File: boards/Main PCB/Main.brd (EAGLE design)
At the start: 101.6 x 76.2 mm, 120 parts, among them CN1 MINIB, CN2 MINIB, IC1 FT232RL, IC2 FT232RL, IC4 OKR-T_3-W12-C, J1 3_PIN_JST-XH, J2 2_PIN_JST-XH, J3 5_PIN_JST-XH, Q4 BSS138, Q5 BSS138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

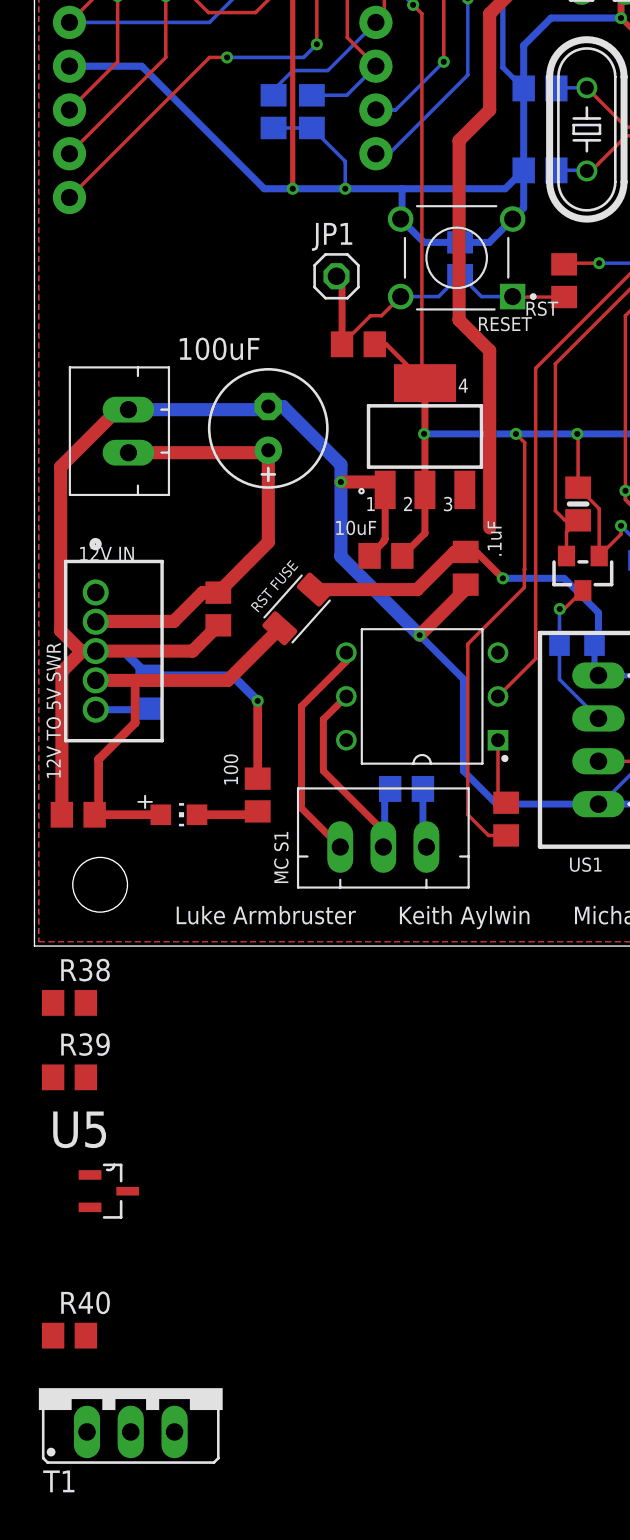
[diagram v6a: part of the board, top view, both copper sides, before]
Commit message: Routed crowbar circuit
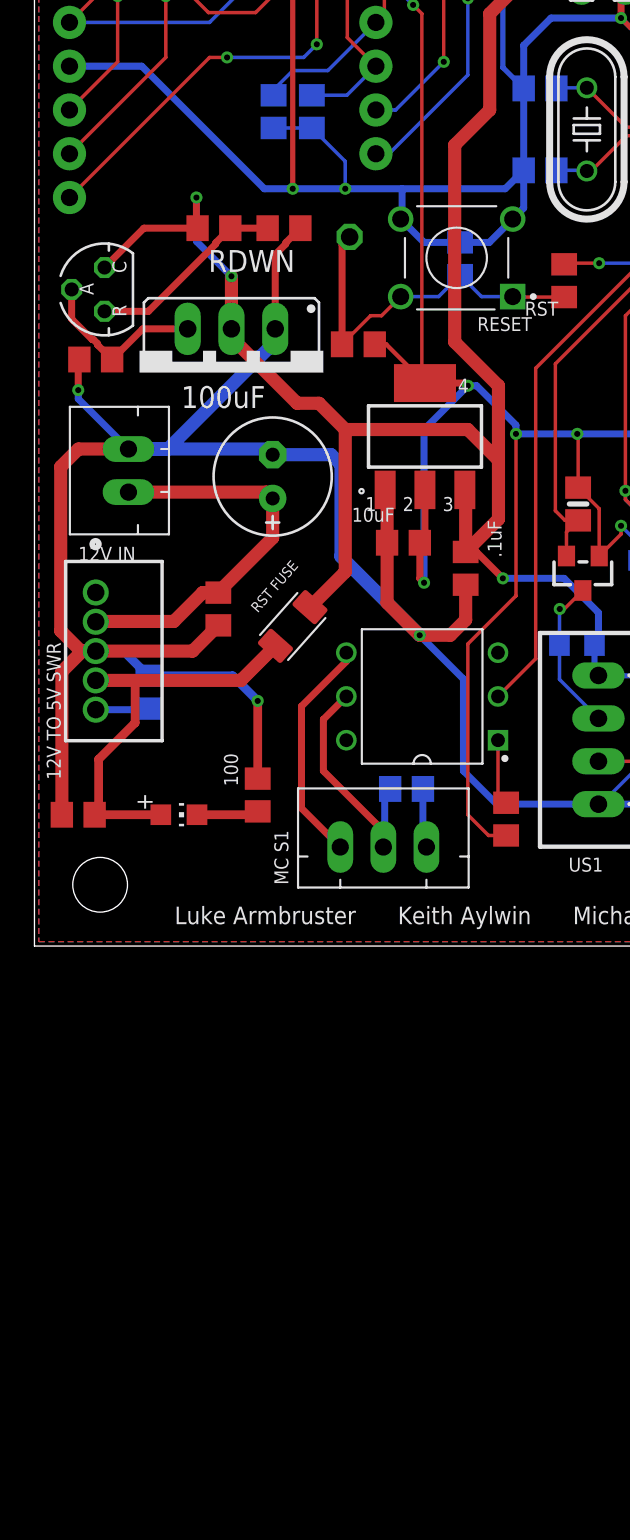
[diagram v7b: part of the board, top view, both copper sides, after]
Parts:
- removed R38, R39: (no value), resistor:R0805
- removed U5: TL431AIDBZTG4, main_library:SOT95P237X112-3N
- added RDWN, RUP: (no value), resistor:R0805
- added VR1: (no value), v-reg:TO92-CLP
- moved T1 59.2 mm to (11.4, 33.3), turned to 180 degrees
- moved R40 56.7 mm to (3.56, 34.0)
- moved C17 2.81 mm to (13.8, 27.2)
- moved JP1 2.41 mm to (18.3, 41.1), flipped to the bottom
- moved J2 2.29 mm to (2.05, 31.3)
- moved C9 1.27 mm to (21.4, 23.4)
- moved R33 1.05 mm to (15.0, 18.5)
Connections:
- removed net N$30: R40.2, T1.G, U5.3
- new net N$24: R40.2, T1.G, VR1.A
- net +5V: now also RUP.2, VR1.C; no longer R38.2, U5.1
- net GND: now also RDWN.1; no longer R39.1
- net N$25: now also RDWN.2, RUP.1, VR1.R; no longer R38.1, R39.2, U5.2
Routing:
- net +5V: track 167.0 -> 210.8 mm, vias 3 -> 5
- net GND: track 764.5 -> 790.5 mm
- net N$25: track 0.00 -> 11.5 mm
- net N$24: track 0.00 -> 10.2 mm
- net +3V3: track 326.9 -> 335.5 mm, vias 21 -> 22
- net RESET: track 19.2 -> 21.5 mm
- net 12V_IN: track 25.4 -> 23.1 mm
- net N$21: track 26.7 -> 26.1 mm

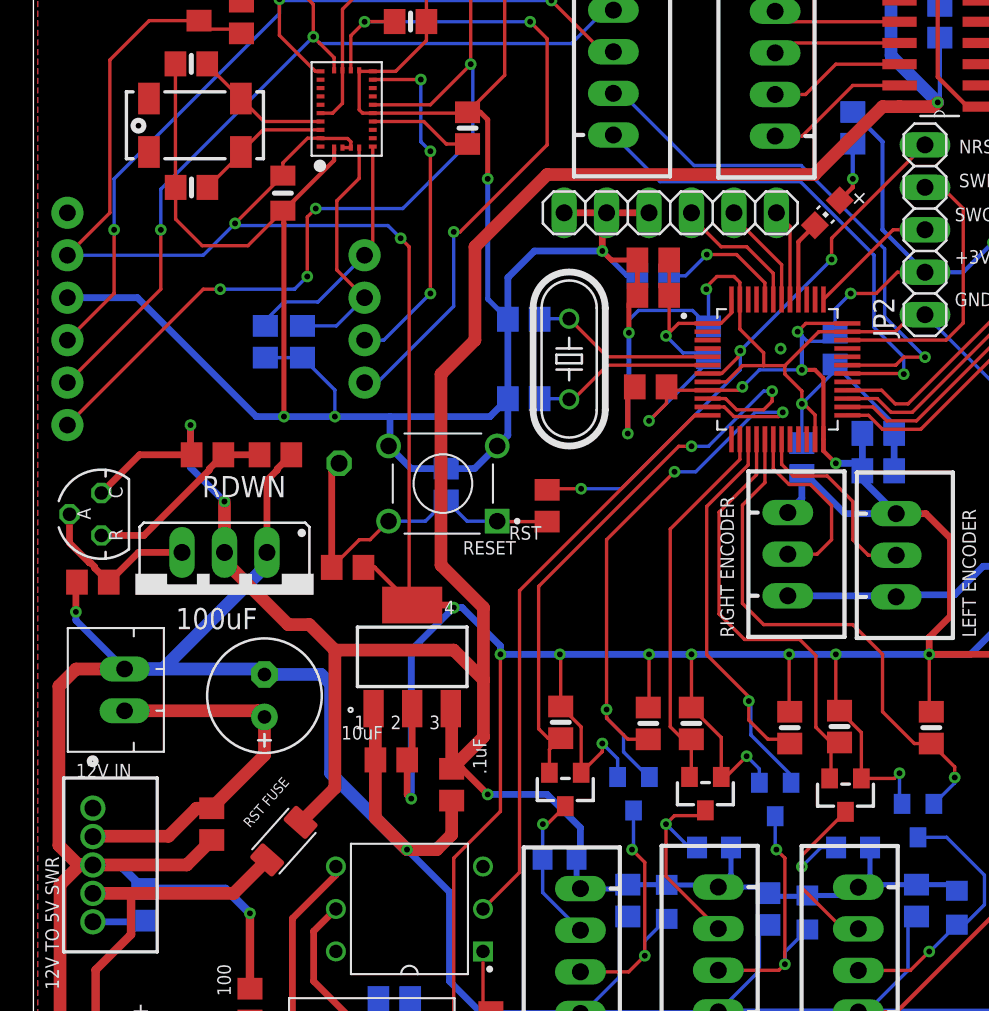
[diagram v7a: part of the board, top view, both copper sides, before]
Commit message: Minor trace routing changes
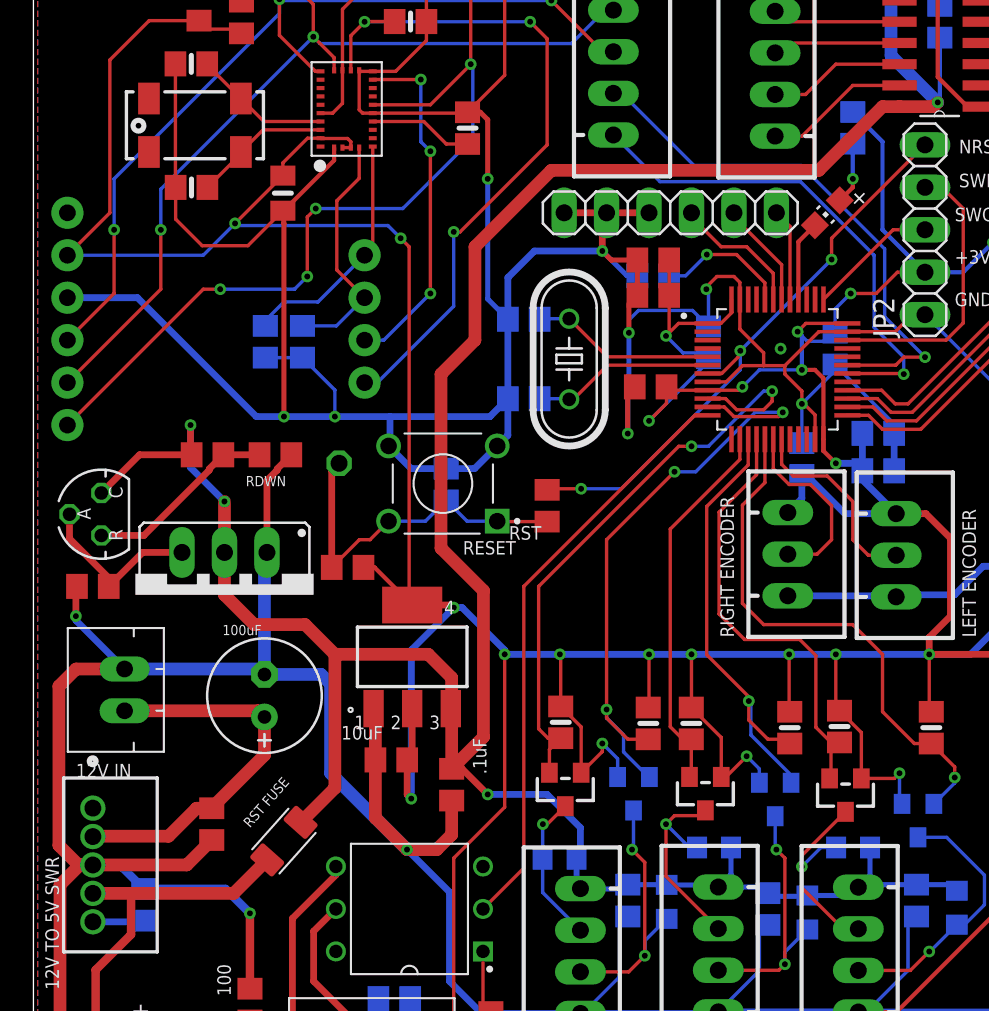
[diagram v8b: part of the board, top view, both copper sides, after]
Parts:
- moved R40 0.25 mm to (3.56, 33.8)
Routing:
- net GND: track 790.5 -> 785.7 mm
- net +5V: track 210.8 -> 211.7 mm
